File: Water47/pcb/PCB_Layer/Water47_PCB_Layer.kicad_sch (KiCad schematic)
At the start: 107 parts, among them SW1 Esc, SW10 O, SW11 P, SW12 -, SW13 Del, SW14 Cmd, SW15 A, SW16 S, SW17 D, SW18 F, SW19 G, SW2 Q, SW20 H, SW21 J, SW22 K, SW23 L, SW24 ;, SW25 Bs, SW26 Shift(L), SW27 Z, SW28 X, SW29 C, SW3 W, SW30 V, SW31 B, SW32 N, SW33 M, SW34 ,, SW35 ., SW36 Shift(R), SW37 Fn, SW38 Ctrl(L), SW39 Win(L), SW4 E, SW40 Alt(L), SW41 Shift(C), SW42 Fn(C), SW43 Enter, SW44 ←, SW45 ↓, SW46 ↑, SW47 →, SW5 R, SW6 T, SW7 Y, SW8 U, SW9 I, U1 MOUDLE-SEEEDUINO-XIAO

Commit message: feat: change micon direction
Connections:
- net PIN2: now also U1.10 (PA5_A9_D9_MISO); no longer U1.9 (PA7_A8_D8_SCK)
- net PIN3: now also U1.9 (PA7_A8_D8_SCK); no longer U1.4 (PA11_A3_D3)
- net PIN4: now also U1.8 (PB09_A7_D7_RX); no longer U1.11 (PA6_A10_D10_MOSI)
- net PIN5: now also U1.11 (PA6_A10_D10_MOSI); no longer U1.3 (PA10_A2_D2)
- net PIN6: now also U1.7 (PB08_A6_D6_TX); no longer U1.10 (PA5_A9_D9_MISO)
- net PIN7: now also U1.4 (PA11_A3_D3); no longer U1.8 (PB09_A7_D7_RX)
- net PIN8: now also U1.2 (PA4_A1_D1); no longer U1.7 (PB08_A6_D6_TX)
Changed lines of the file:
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@@
   (junction (at 71.12 163.83) (diameter 0) (color 0 0 0 0)
   )
-  (no_connect (at 54.61 33.02))
+  (no_connect (at 54.61 35.56))
   (wire (pts (xy 124.46 135.89) (xy 144.78 135.89))
     (stroke (width 0) (type default) (color 0 0 0 0))
@@
     )
   )
-  (global_label "PIN2" (shape input) (at 95.25 43.18 0) (fields_autoplaced)
+  (global_label "PIN1" (shape input) (at 54.61 30.48 180) (fields_autoplaced)
+    (effects (font (size 1.27 1.27)) (justify right))
+    (property "Intersheet References" "${INTERSHEET_REFS}" (id 0) (at 47.871 30.4006 0)
+      (effects (font (size 1.27 1.27)) (justify right) hide)
+    )
+  )
+  (global_label "PIN1" (shape input) (at 45.72 82.55 180) (fields_autoplaced)
+    (effects (font (size 1.27 1.27)) (justify right))
+    (property "Intersheet References" "${INTERSHEET_REFS}" (id 0) (at 38.981 82.4706 0)
+      (effects (font (size 1.27 1.27)) (justify right) hide)
+    )
+  )
+  (global_label "PIN7" (shape input) (at 54.61 38.1 180) (fields_autoplaced)
+    (effects (font (size 1.27 1.27)) (justify right))
+    (property "Intersheet References" "${INTERSHEET_REFS}" (id 0) (at 47.871 38.1794 0)
+      (effects (font (size 1.27 1.27)) (justify right) hide)
+    )
+  )
+  (global_label "PIN4" (shape input) (at 95.25 45.72 0) (fields_autoplaced)
     (effects (font (size 1.27 1.27)) (justify left))
-    (property "Intersheet References" "${INTERSHEET_REFS}" (id 0) (at 101.989 43.2594 0)
+    (property "Intersheet References" "${INTERSHEET_REFS}" (id 0) (at 101.989 45.6406 0)
       (effects (font (size 1.27 1.27)) (justify left) hide)
     )
   )
-  (global_label "PIN1" (shape input) (at 45.72 82.55 180) (fields_autoplaced)
-    (effects (font (size 1.27 1.27)) (justify right))
-    (property "Intersheet References" "${INTERSHEET_REFS}" (id 0) (at 38.981 82.4706 0)
-      (effects (font (size 1.27 1.27)) (justify right) hide)
-    )
-  )
-  (global_label "PIN4" (shape input) (at 95.25 38.1 0) (fields_autoplaced)
+  (global_label "PIN6" (shape input) (at 54.61 45.72 180) (fields_autoplaced)
+    (effects (font (size 1.27 1.27)) (justify right))
+    (property "Intersheet References" "${INTERSHEET_REFS}" (id 0) (at 47.871 45.6406 0)
+      (effects (font (size 1.27 1.27)) (justify right) hide)
+    )
+  )
+  (global_label "PIN5" (shape input) (at 95.25 38.1 0) (fields_autoplaced)
     (effects (font (size 1.27 1.27)) (justify left))
     (property "Intersheet References" "${INTERSHEET_REFS}" (id 0) (at 101.989 38.1794 0)
@@
     )
   )
-  (global_label "PIN6" (shape input) (at 95.25 40.64 0) (fields_autoplaced)
+  (global_label "PIN2" (shape input) (at 45.72 100.33 180) (fields_autoplaced)
+    (effects (font (size 1.27 1.27)) (justify right))
+    (property "Intersheet References" "${INTERSHEET_REFS}" (id 0) (at 38.981 100.2506 0)
+      (effects (font (size 1.27 1.27)) (justify right) hide)
+    )
+  )
+  (global_label "PIN5" (shape input) (at 45.72 153.67 180) (fields_autoplaced)
+    (effects (font (size 1.27 1.27)) (justify right))
+    (property "Intersheet References" "${INTERSHEET_REFS}" (id 0) (at 38.981 153.5906 0)
+      (effects (font (size 1.27 1.27)) (justify right) hide)
+    )
+  )
+  (global_label "PIN3" (shape input) (at 45.72 118.11 180) (fields_autoplaced)
+    (effects (font (size 1.27 1.27)) (justify right))
+    (property "Intersheet References" "${INTERSHEET_REFS}" (id 0) (at 38.981 118.0306 0)
+      (effects (font (size 1.27 1.27)) (justify right) hide)
+    )
+  )
+  (global_label "PIN7" (shape input) (at 45.72 189.23 180) (fields_autoplaced)
+    (effects (font (size 1.27 1.27)) (justify right))
+    (property "Intersheet References" "${INTERSHEET_REFS}" (id 0) (at 38.981 189.1506 0)
+      (effects (font (size 1.27 1.27)) (justify right) hide)
+    )
+  )
+  (global_label "PIN2" (shape input) (at 95.25 40.64 0) (fields_autoplaced)
     (effects (font (size 1.27 1.27)) (justify left))
-    (property "Intersheet References" "${INTERSHEET_REFS}" (id 0) (at 101.989 40.5606 0)
+    (property "Intersheet References" "${INTERSHEET_REFS}" (id 0) (at 101.989 40.7194 0)
       (effects (font (size 1.27 1.27)) (justify left) hide)
     )
   )
-  (global_label "PIN2" (shape input) (at 45.72 100.33 180) (fields_autoplaced)
-    (effects (font (size 1.27 1.27)) (justify right))
-    (property "Intersheet References" "${INTERSHEET_REFS}" (id 0) (at 38.981 100.2506 0)
-      (effects (font (size 1.27 1.27)) (justify right) hide)
-    )
-  )
-  (global_label "PIN7" (shape input) (at 95.25 45.72 0) (fields_autoplaced)
+  (global_label "SDA" (shape input) (at 54.61 40.64 180) (fields_autoplaced)
+    (effects (font (size 1.27 1.27)) (justify right))
+    (property "Intersheet References" "${INTERSHEET_REFS}" (id 0) (at 48.7177 40.5606 0)
+      (effects (font (size 1.27 1.27)) (justify right) hide)
+    )
+  )
+  (global_label "PIN6" (shape input) (at 45.72 171.45 180) (fields_autoplaced)
+    (effects (font (size 1.27 1.27)) (justify right))
+    (property "Intersheet References" "${INTERSHEET_REFS}" (id 0) (at 38.981 171.3706 0)
+      (effects (font (size 1.27 1.27)) (justify right) hide)
+    )
+  )
+  (global_label "PIN3" (shape input) (at 95.25 43.18 0) (fields_autoplaced)
     (effects (font (size 1.27 1.27)) (justify left))
-    (property "Intersheet References" "${INTERSHEET_REFS}" (id 0) (at 101.989 45.6406 0)
+    (property "Intersheet References" "${INTERSHEET_REFS}" (id 0) (at 101.989 43.1006 0)
       (effects (font (size 1.27 1.27)) (justify left) hide)
     )
   )
-  (global_label "PIN5" (shape input) (at 45.72 153.67 180) (fields_autoplaced)
-    (effects (font (size 1.27 1.27)) (justify right))
-    (property "Intersheet References" "${INTERSHEET_REFS}" (id 0) (at 38.981 153.5906 0)
-      (effects (font (size 1.27 1.27)) (justify right) hide)
-    )
-  )
-  (global_label "PIN3" (shape input) (at 45.72 118.11 180) (fields_autoplaced)
-    (effects (font (size 1.27 1.27)) (justify right))
-    (property "Intersheet References" "${INTERSHEET_REFS}" (id 0) (at 38.981 118.0306 0)
-      (effects (font (size 1.27 1.27)) (justify right) hide)
-    )
-  )
-  (global_label "PIN1" (shape input) (at 54.61 30.48 180) (fields_autoplaced)
-    (effects (font (size 1.27 1.27)) (justify right))
-    (property "Intersheet References" "${INTERSHEET_REFS}" (id 0) (at 47.871 30.4006 0)
-      (effects (font (size 1.27 1.27)) (justify right) hide)
-    )
-  )
-  (global_label "PIN7" (shape input) (at 45.72 189.23 180) (fields_autoplaced)
-    (effects (font (size 1.27 1.27)) (justify right))
-    (property "Intersheet References" "${INTERSHEET_REFS}" (id 0) (at 38.981 189.1506 0)
-      (effects (font (size 1.27 1.27)) (justify right) hide)
-    )
-  )
-  (global_label "PIN5" (shape input) (at 54.61 35.56 180) (fields_autoplaced)
-    (effects (font (size 1.27 1.27)) (justify right))
-    (property "Intersheet References" "${INTERSHEET_REFS}" (id 0) (at 47.871 35.4806 0)
-      (effects (font (size 1.27 1.27)) (justify right) hide)
-    )
-  )
-  (global_label "PIN3" (shape input) (at 54.61 38.1 180) (fields_autoplaced)
-    (effects (font (size 1.27 1.27)) (justify right))
-    (property "Intersheet References" "${INTERSHEET_REFS}" (id 0) (at 47.871 38.0206 0)
-      (effects (font (size 1.27 1.27)) (justify right) hide)
-    )
-  )
-  (global_label "SDA" (shape input) (at 54.61 40.64 180) (fields_autoplaced)
-    (effects (font (size 1.27 1.27)) (justify right))
-    (property "Intersheet References" "${INTERSHEET_REFS}" (id 0) (at 48.7177 40.5606 0)
-      (effects (font (size 1.27 1.27)) (justify right) hide)
-    )
-  )
-  (global_label "PIN6" (shape input) (at 45.72 171.45 180) (fields_autoplaced)
-    (effects (font (size 1.27 1.27)) (justify right))
-    (property "Intersheet References" "${INTERSHEET_REFS}" (id 0) (at 38.981 171.3706 0)
-      (effects (font (size 1.27 1.27)) (justify right) hide)
-    )
-  )
-  (global_label "PIN8" (shape input) (at 54.61 45.72 180) (fields_autoplaced)
-    (effects (font (size 1.27 1.27)) (justify right))
-    (property "Intersheet References" "${INTERSHEET_REFS}" (id 0) (at 47.871 45.7994 0)
-      (effects (font (size 1.27 1.27)) (justify right) hide)
-    )
-  )
   (global_label "PIN4" (shape input) (at 45.72 135.89 180) (fields_autoplaced)
     (effects (font (size 1.27 1.27)) (justify right))
@@
       (effects (font (size 1.27 1.27)) (justify right) hide)
     )
+  )
+  (global_label "PIN8" (shape input) (at 54.61 33.02 180) (fields_autoplaced)
+    (effects (font (size 1.27 1.27)) (justify right))
+    (property "Intersheet References" "${INTERSHEET_REFS}" (id 0) (at 47.871 33.0994 0)
+      (effects (font (size 1.27 1.27)) (justify right) hide)
+    )

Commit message: feat: change mounting spacer to hex
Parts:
- H1, H2, H3, H4: footprint kbd_Hole:m2_Screw_Hole -> kbd_Hole:m2_Spacer_Hole_hex
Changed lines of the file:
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@@
       (effects (font (size 1.27 1.27)) (justify left))
     )
-    (property "Footprint" "kbd_Hole:m2_Screw_Hole" (id 2) (at 22.86 68.58 0)
+    (property "Footprint" "kbd_Hole:m2_Spacer_Hole_hex" (id 2) (at 22.86 68.58 0)
       (effects (font (size 1.27 1.27)) hide)
     )
@@
       (effects (font (size 1.27 1.27)) (justify left))
     )
-    (property "Footprint" "kbd_Hole:m2_Screw_Hole" (id 2) (at 29.21 218.44 0)
+    (property "Footprint" "kbd_Hole:m2_Spacer_Hole_hex" (id 2) (at 29.21 218.44 0)
       (effects (font (size 1.27 1.27)) hide)
     )
@@
       (effects (font (size 1.27 1.27)) (justify left))
     )
-    (property "Footprint" "kbd_Hole:m2_Screw_Hole" (id 2) (at 212.09 217.17 0)
+    (property "Footprint" "kbd_Hole:m2_Spacer_Hole_hex" (id 2) (at 212.09 217.17 0)
       (effects (font (size 1.27 1.27)) hide)
     )
@@
       (effects (font (size 1.27 1.27)) (justify left))
     )
-    (property "Footprint" "kbd_Hole:m2_Screw_Hole" (id 2) (at 217.17 63.5 0)
+    (property "Footprint" "kbd_Hole:m2_Spacer_Hole_hex" (id 2) (at 217.17 63.5 0)
       (effects (font (size 1.27 1.27)) hide)
     )
@@
     )
     (path "/17fe6c74-7093-4ce3-b0e5-cd6b76f5155b"
-      (reference "H1") (unit 1) (value "MountingHole") (footprint "kbd_Hole:m2_Screw_Hole")
+      (reference "H1") (unit 1) (value "MountingHole") (footprint "kbd_Hole:m2_Spacer_Hole_hex")
     )
     (path "/bbde9b31-2ca1-42cc-a23f-bd08fc375c76"
-      (reference "H2") (unit 1) (value "MountingHole") (footprint "kbd_Hole:m2_Screw_Hole")
+      (reference "H2") (unit 1) (value "MountingHole") (footprint "kbd_Hole:m2_Spacer_Hole_hex")
     )
     (path "/f64ccafc-8d73-4e0d-a0a9-52c38f87dc6c"
-      (reference "H3") (unit 1) (value "MountingHole") (footprint "kbd_Hole:m2_Screw_Hole")
+      (reference "H3") (unit 1) (value "MountingHole") (footprint "kbd_Hole:m2_Spacer_Hole_hex")
     )
     (path "/caa5335b-ab47-478f-b510-96296c076797"
-      (reference "H4") (unit 1) (value "MountingHole") (footprint "kbd_Hole:m2_Screw_Hole")
+      (reference "H4") (unit 1) (value "MountingHole") (footprint "kbd_Hole:m2_Spacer_Hole_hex")
     )
     (path "/f2c71871-836d-493d-97ca-9ecc25d8c3ed"

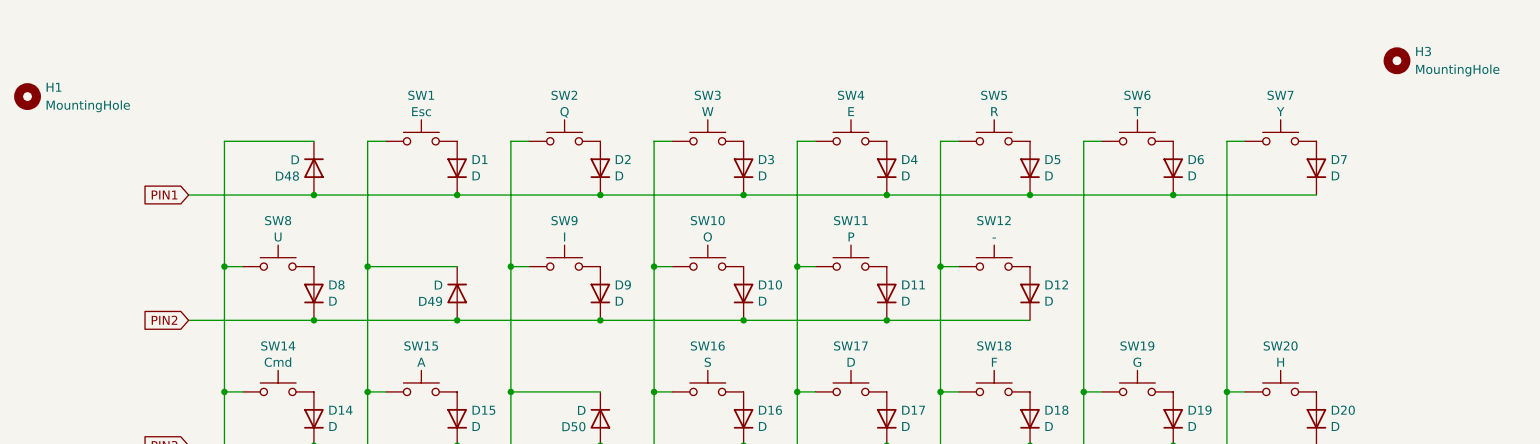
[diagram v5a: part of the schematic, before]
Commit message: feat: add mounting hole, set gerber path
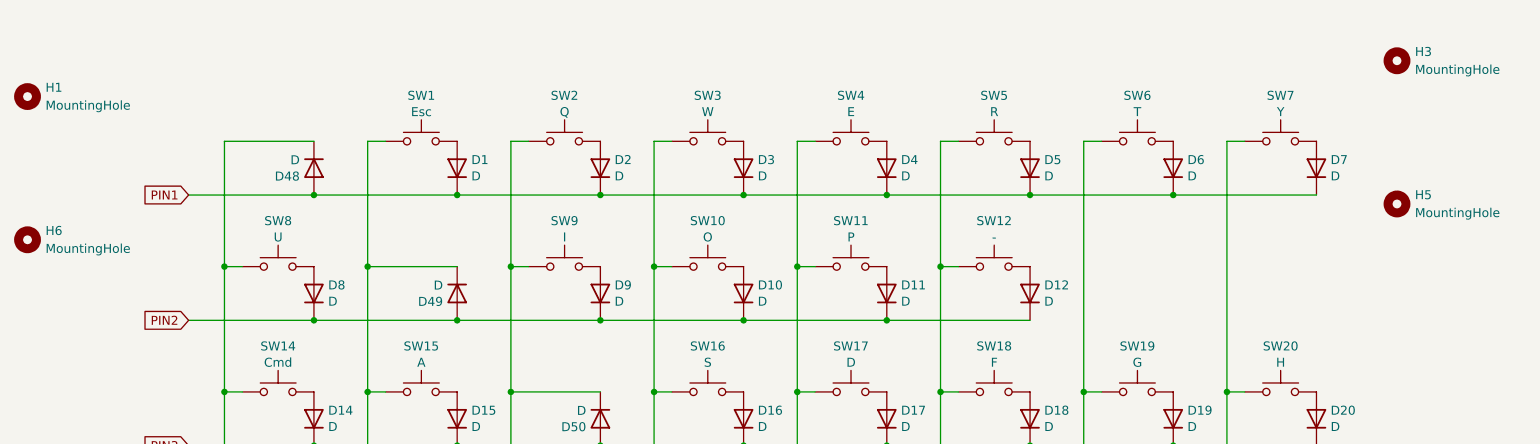
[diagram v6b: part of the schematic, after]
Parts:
- added H5, H6: MountingHole, kbd_Hole:m2_Spacer_Hole_hex, symbol Mechanical:MountingHole
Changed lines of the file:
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@@
     (pin "2")
+  )
+  (symbol (lib_id "Mechanical:MountingHole") (at 22.86 88.9 0) (unit 1)
+    (in_bom yes) (on_board yes) (fields_autoplaced)
+    (property "Reference" "H6" (id 0) (at 25.4 87.6299 0)
+      (effects (font (size 1.27 1.27)) (justify left))
+    )
+    (property "Value" "MountingHole" (id 1) (at 25.4 90.1699 0)
+      (effects (font (size 1.27 1.27)) (justify left))
+    )
+    (property "Footprint" "kbd_Hole:m2_Spacer_Hole_hex" (id 2) (at 22.86 88.9 0)
+      (effects (font (size 1.27 1.27)) hide)
+    )
+    (property "Datasheet" "~" (id 3) (at 22.86 88.9 0)
+      (effects (font (size 1.27 1.27)) hide)
+    )
   )
   (symbol (lib_id "Device:D") (at 144.78 114.3 90) (unit 1)
@@
     (pin "1")
     (pin "2")
+  )
+  (symbol (lib_id "Mechanical:MountingHole") (at 217.17 83.82 0) (unit 1)
+    (in_bom yes) (on_board yes) (fields_autoplaced)
+    (property "Reference" "H5" (id 0) (at 219.71 82.5499 0)
+      (effects (font (size 1.27 1.27)) (justify left))
+    )
+    (property "Value" "MountingHole" (id 1) (at 219.71 85.0899 0)
+      (effects (font (size 1.27 1.27)) (justify left))
+    )
+    (property "Footprint" "kbd_Hole:m2_Spacer_Hole_hex" (id 2) (at 217.17 83.82 0)
+      (effects (font (size 1.27 1.27)) hide)
+    )
+    (property "Datasheet" "~" (id 3) (at 217.17 83.82 0)
+      (effects (font (size 1.27 1.27)) hide)
+    )
   )
   (symbol (lib_id "Mechanical:MountingHole") (at 212.09 217.17 0) (unit 1)
@@
       (reference "H4") (unit 1) (value "MountingHole") (footprint "kbd_Hole:m2_Spacer_Hole_hex")
     )
+    (path "/c86ad271-32d9-470c-acca-11205bab3dad"
+      (reference "H5") (unit 1) (value "MountingHole") (footprint "kbd_Hole:m2_Spacer_Hole_hex")
+    )
+    (path "/c082bbe0-d6b3-4502-baf1-7b84650c5f86"
+      (reference "H6") (unit 1) (value "MountingHole") (footprint "kbd_Hole:m2_Spacer_Hole_hex")
+    )
     (path "/f2c71871-836d-493d-97ca-9ecc25d8c3ed"
